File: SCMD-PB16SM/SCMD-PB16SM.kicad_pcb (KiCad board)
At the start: 2 copper layers, 200 x 100 mm, 68 parts, among them J1 Logic Supply, M1 SCMD, M10 SCMD, M11 SCMD, M12 SCMD, M2 SCMD, M3 SCMD, M4 SCMD, M5 SCMD, M6 SCMD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

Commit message: Add files via upload
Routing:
- net (no net): vias 0 -> 4

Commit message: Add files via upload
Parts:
- moved D10 0.25 mm to (184.5, 107.6)
- moved D11 0.25 mm to (199.1, 107.6)
- moved D12 0.25 mm to (213.7, 107.6)
- moved D13 0.25 mm to (46.0, 40.1)
- moved D14 0.25 mm to (41.0, 36.8)
- moved D15 0.25 mm to (34.4, 34.9)
- moved D2 0.25 mm to (69.9, 107.6)
- moved D3 0.25 mm to (84.2, 107.6)
- moved D5 0.25 mm to (112.8, 107.6)
- moved D6 0.25 mm to (127.1, 107.6)
- moved D7 0.25 mm to (141.3, 107.6)
- moved D8 0.25 mm to (155.7, 107.6)
- moved D9 0.25 mm to (170.1, 107.6)
- moved F1 0.25 mm to (55.3, 35.6)
- moved F10 0.25 mm to (182.7, 35.6)
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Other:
- board size 200 x 100 mm -> 200 x 101 mm

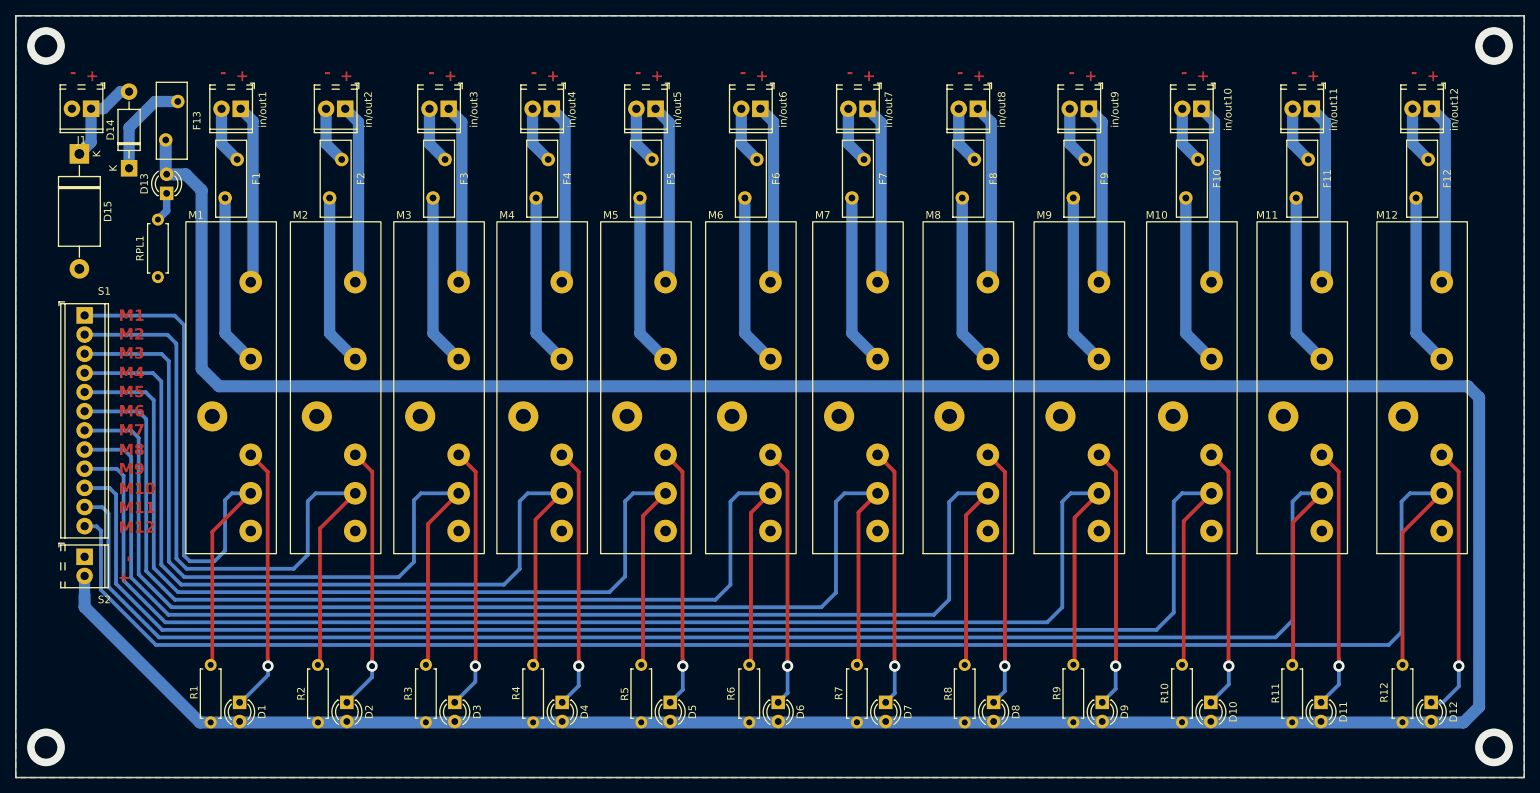
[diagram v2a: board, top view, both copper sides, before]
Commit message: Add files via upload
ADD PCINT INTERUP
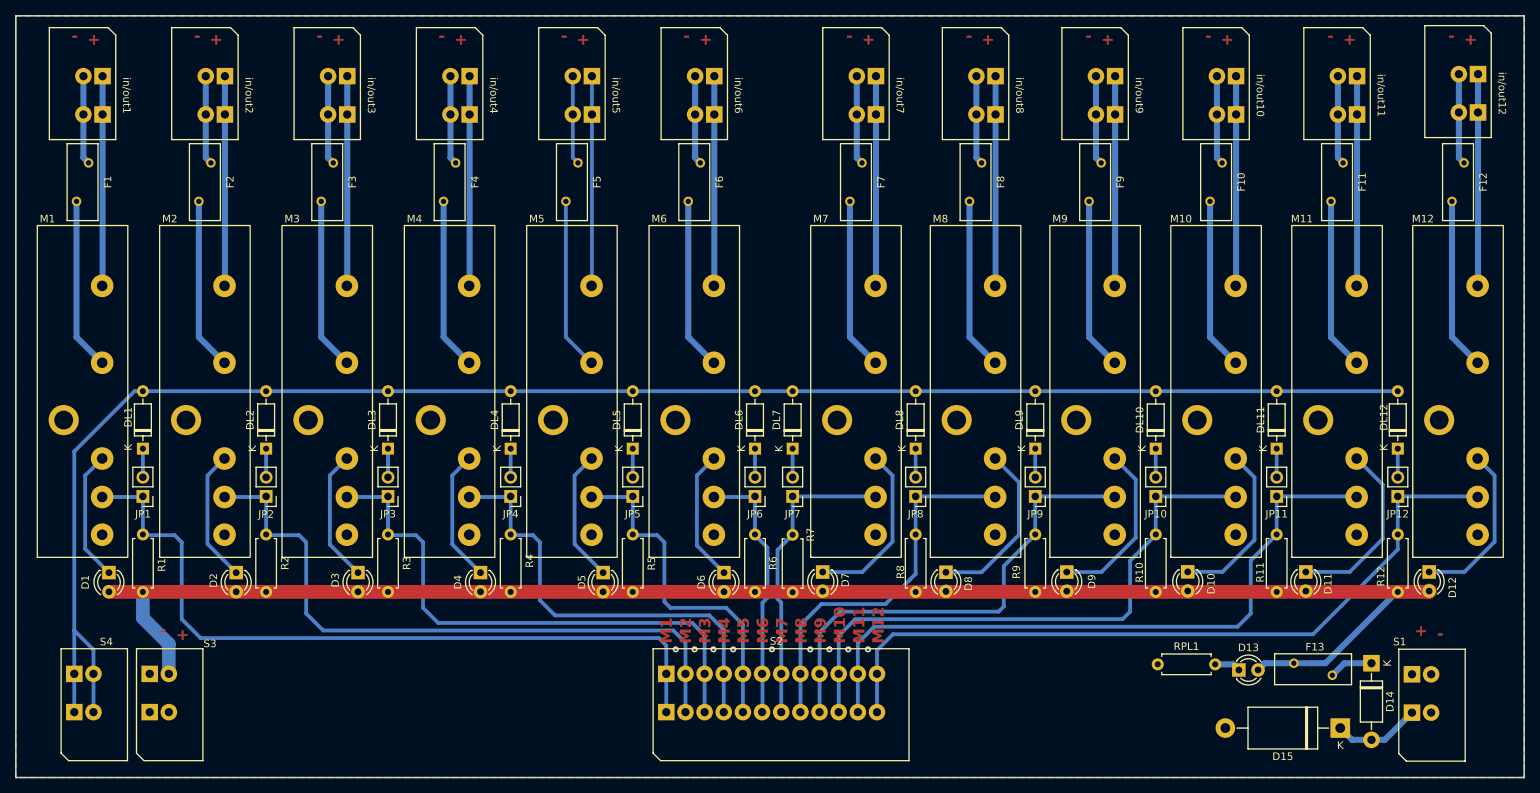
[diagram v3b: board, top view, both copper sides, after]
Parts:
- added DL1: 1N4148, Diode_THT:D_DO-35_SOD27_P7.62mm_Horizontal, F.Cu at (42.8, 73.9)
- added DL10: 1N4148, Diode_THT:D_DO-35_SOD27_P7.62mm_Horizontal, F.Cu at (177.2, 73.9)
- added DL11: 1N4148, Diode_THT:D_DO-35_SOD27_P7.62mm_Horizontal, F.Cu at (193.2, 73.9)
- added DL12: 1N4148, Diode_THT:D_DO-35_SOD27_P7.62mm_Horizontal, F.Cu at (209.2, 73.9)
- added DL2: 1N4148, Diode_THT:D_DO-35_SOD27_P7.62mm_Horizontal, F.Cu at (59.2, 73.9)
- added DL3: 1N4148, Diode_THT:D_DO-35_SOD27_P7.62mm_Horizontal, F.Cu at (75.3, 73.9)
- added DL4: 1N4148, Diode_THT:D_DO-35_SOD27_P7.62mm_Horizontal, F.Cu at (91.6, 73.9)
- added DL5: 1N4148, Diode_THT:D_DO-35_SOD27_P7.62mm_Horizontal, F.Cu at (107.8, 73.9)
- added DL6: 1N4148, Diode_THT:D_DO-35_SOD27_P7.62mm_Horizontal, F.Cu at (124.0, 73.9)
- added DL7: 1N4148, Diode_THT:D_DO-35_SOD27_P7.62mm_Horizontal, F.Cu at (129.0, 73.9)
- added DL8: 1N4148, Diode_THT:D_DO-35_SOD27_P7.62mm_Horizontal, F.Cu at (145.3, 73.9)
- added DL9: 1N4148, Diode_THT:D_DO-35_SOD27_P7.62mm_Horizontal, F.Cu at (161.2, 73.9)
- added JP1: PCIN Init, Connector_PinHeader_2.54mm:PinHeader_1x02_P2.54mm_Vertical, F.Cu at (42.8, 80.3)
- added JP10: PCIN Init, Connector_PinHeader_2.54mm:PinHeader_1x02_P2.54mm_Vertical, F.Cu at (177.2, 80.3)
- added JP11: PCIN Init, Connector_PinHeader_2.54mm:PinHeader_1x02_P2.54mm_Vertical, F.Cu at (193.2, 80.3)
- added JP12: PCIN Init, Connector_PinHeader_2.54mm:PinHeader_1x02_P2.54mm_Vertical, F.Cu at (209.2, 80.3)
- added JP2: PCIN Init, Connector_PinHeader_2.54mm:PinHeader_1x02_P2.54mm_Vertical, F.Cu at (59.2, 80.3)
- added JP3: PCIN Init, Connector_PinHeader_2.54mm:PinHeader_1x02_P2.54mm_Vertical, F.Cu at (75.3, 80.3)
- added JP4: PCIN Init, Connector_PinHeader_2.54mm:PinHeader_1x02_P2.54mm_Vertical, F.Cu at (91.6, 80.3)
- added JP5: PCIN Init, Connector_PinHeader_2.54mm:PinHeader_1x02_P2.54mm_Vertical, F.Cu at (107.8, 80.3)
- added JP6: PCIN Init, Connector_PinHeader_2.54mm:PinHeader_1x02_P2.54mm_Vertical, F.Cu at (124.0, 80.3)
- added JP7: PCIN Init, Connector_PinHeader_2.54mm:PinHeader_1x02_P2.54mm_Vertical, F.Cu at (129.0, 80.3)
- added JP8: PCIN Init, Connector_PinHeader_2.54mm:PinHeader_1x02_P2.54mm_Vertical, F.Cu at (145.3, 80.3)
- added JP9: PCIN Init, Connector_PinHeader_2.54mm:PinHeader_1x02_P2.54mm_Vertical, F.Cu at (161.2, 80.3)
- added S4: KF141R-2.54-02P-14, TerminalBlock_Series_KF141R:KF141R-2.54-02P-14 (DG141R-2.54-02P-14), F.Cu at (32.6, 106.3)
- S1: renamed from J1; footprint TerminalBlock_Phoenix:TerminalBlock_Phoenix_MPT-0,5-2-2.54_1x02_P2.54mm_Horizontal -> TerminalBlock_Series_KF141R:KF141R-2.54-02P-14 (DG141R-2.54-02P-14)
- S2: renamed from S1; value Screw_Terminal_01x02 -> KF141R-2.54-12P-14; footprint TerminalBlock_Phoenix:TerminalBlock_Phoenix_MPT-0,5-12-2.54_1x12_P2.54mm_Horizontal -> TerminalBlock_Series_KF141R:KF141R-2.54-12P-14 (DG141R-2.54-12P-14)
- S3: renamed from S2; value Screw_Terminal_01x02 -> KF141R-2.54-02P-14; footprint TerminalBlock_Phoenix:TerminalBlock_Phoenix_MPT-0,5-2-2.54_1x02_P2.54mm_Horizontal -> TerminalBlock_Series_KF141R:KF141R-2.54-02P-14 (DG141R-2.54-02P-14)
- in/out1, in/out10, in/out11, in/out12, in/out2, in/out3, in/out4, in/out5, in/out6, in/out7, in/out8, in/out9: value Screw_Terminal_01x02 -> KF141R-2.54-02P-14; footprint TerminalBlock_Phoenix:TerminalBlock_Phoenix_MPT-0,5-2-2.54_1x02_P2.54mm_Horizontal -> TerminalBlock_Series_KF141R:KF141R-2.54-02P-14 (DG141R-2.54-02P-14)
- moved S1 190.4 mm to (209.9, 106.4), turned to 0 degrees
- moved D15 183.7 mm to (201.6, 111.0), turned to 180 degrees
- moved D14 177.3 mm to (205.8, 102.4), turned to -90 degrees
- moved F13 170.9 mm to (200.6, 104.0), turned to 180 degrees
- moved D13 155.6 mm to (188.2, 103.3), turned to 0 degrees
- moved RPL1 142.2 mm to (177.4, 102.5), turned to 0 degrees
- moved S2 90.8 mm to (110.9, 106.3), turned to 0 degrees
- moved D1 24.4 mm to (38.3, 90.4)
- moved D2 22.6 mm to (55.2, 90.4)
- moved D3 21.5 mm to (71.4, 90.4)
- moved D4 20.3 mm to (87.6, 90.4)
- moved M1 19.7 mm to (34.8, 66.3)
- moved F1 19.7 mm to (35.6, 36.0)
- moved S3 19.5 mm to (42.6, 106.3), turned to 0 degrees
- moved R1 19.5 mm to (42.8, 85.3)
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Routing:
- net VCC: track 442.0 -> 210.2 mm
- net /J3-27: track 0.00 -> 225.3 mm
- net /J3-26: track 234.5 -> 100.7 mm
- net /J3-24: track 218.5 -> 90.5 mm
- net /J3-20: track 190.6 -> 63.3 mm
- net /J3-22: track 204.7 -> 77.5 mm
- net /J3-18: track 176.6 -> 50.5 mm
- net /J3-16: track 162.7 -> 40.7 mm
- net /J3-14: track 149.4 -> 35.0 mm
- net /J3-12: track 136.4 -> 46.3 mm
- net /J3-10: track 123.8 -> 59.5 mm
- net /J3-8: track 111.4 -> 73.3 mm
- net Net-(D1-K): track 34.6 -> 17.4 mm, vias 1 -> 0
- net Net-(D2-K): track 34.3 -> 17.6 mm, vias 1 -> 0
- net Net-(D3-K): track 34.1 -> 17.6 mm, vias 1 -> 0
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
